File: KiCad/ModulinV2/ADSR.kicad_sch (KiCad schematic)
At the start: 71 parts, among them IC48 TL074HIDR, IC49 AS3310D, IC50 AS3310D

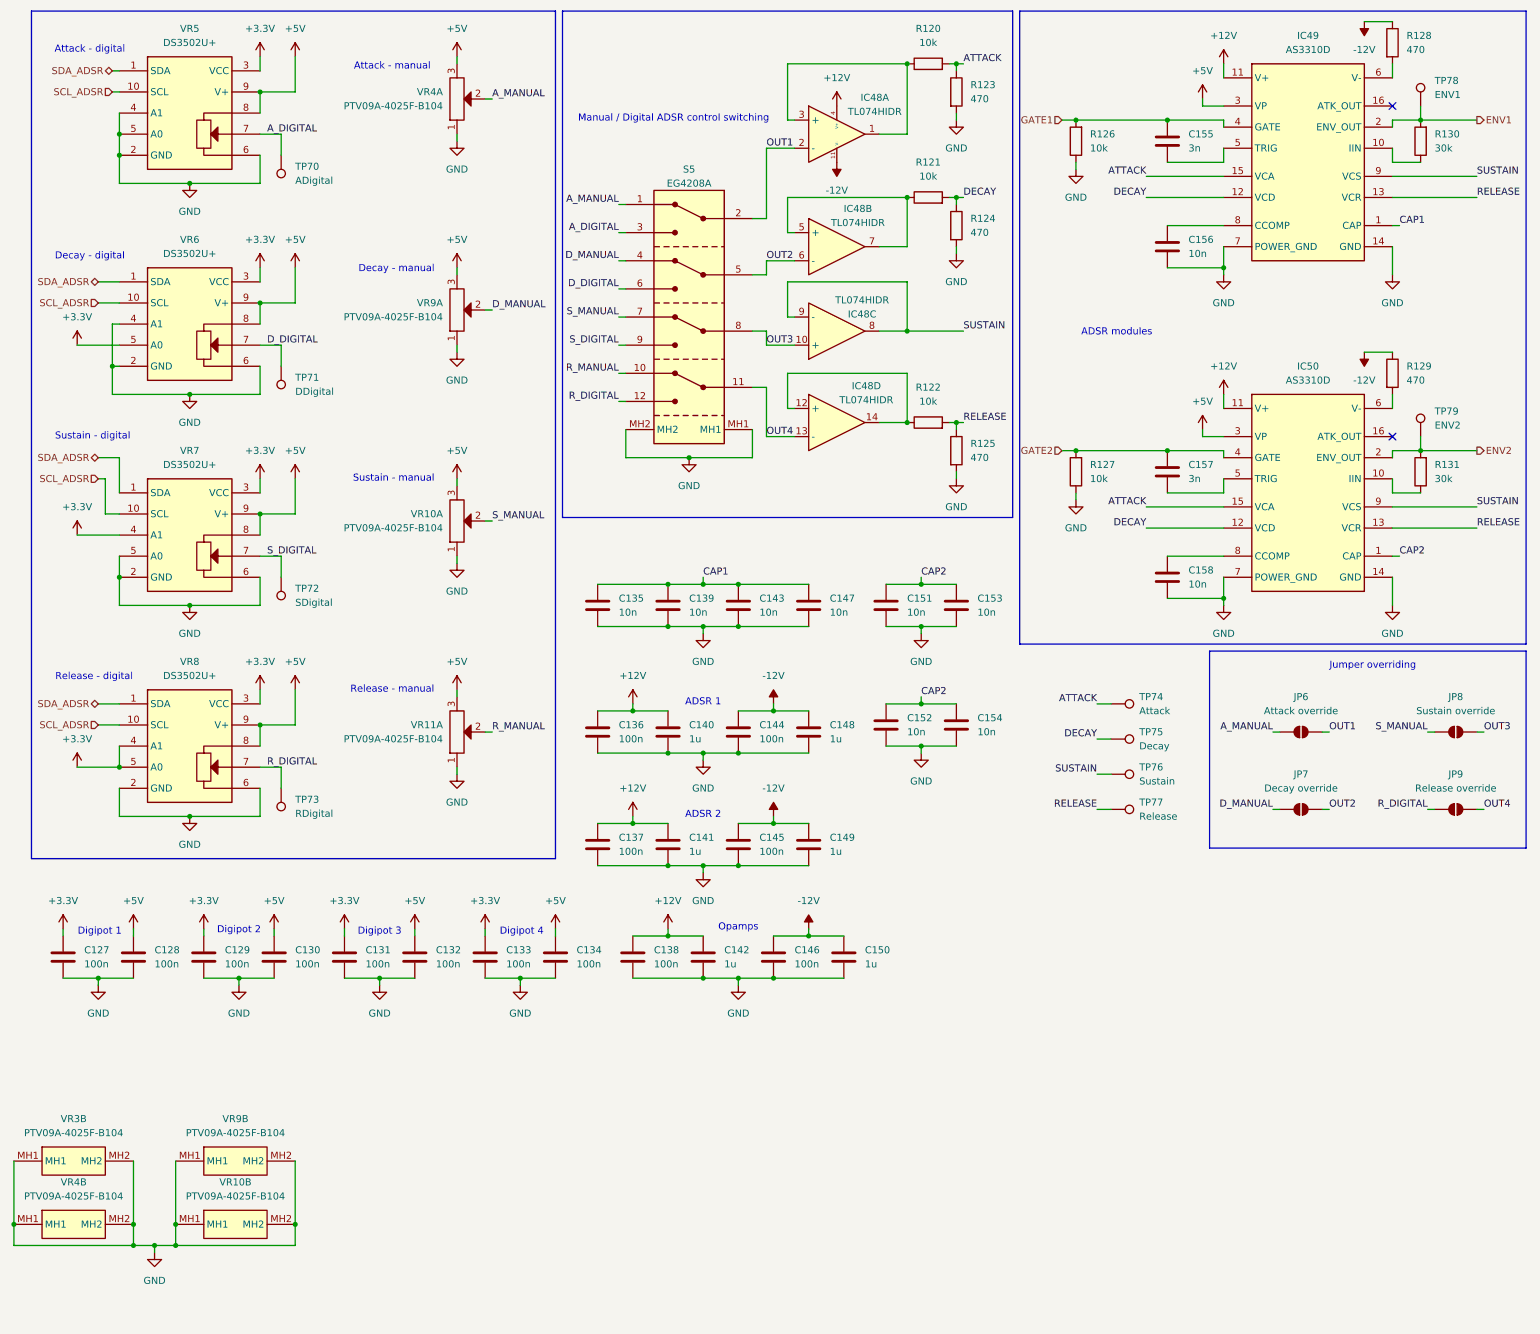
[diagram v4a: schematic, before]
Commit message: Finished Schematic, started on PCB
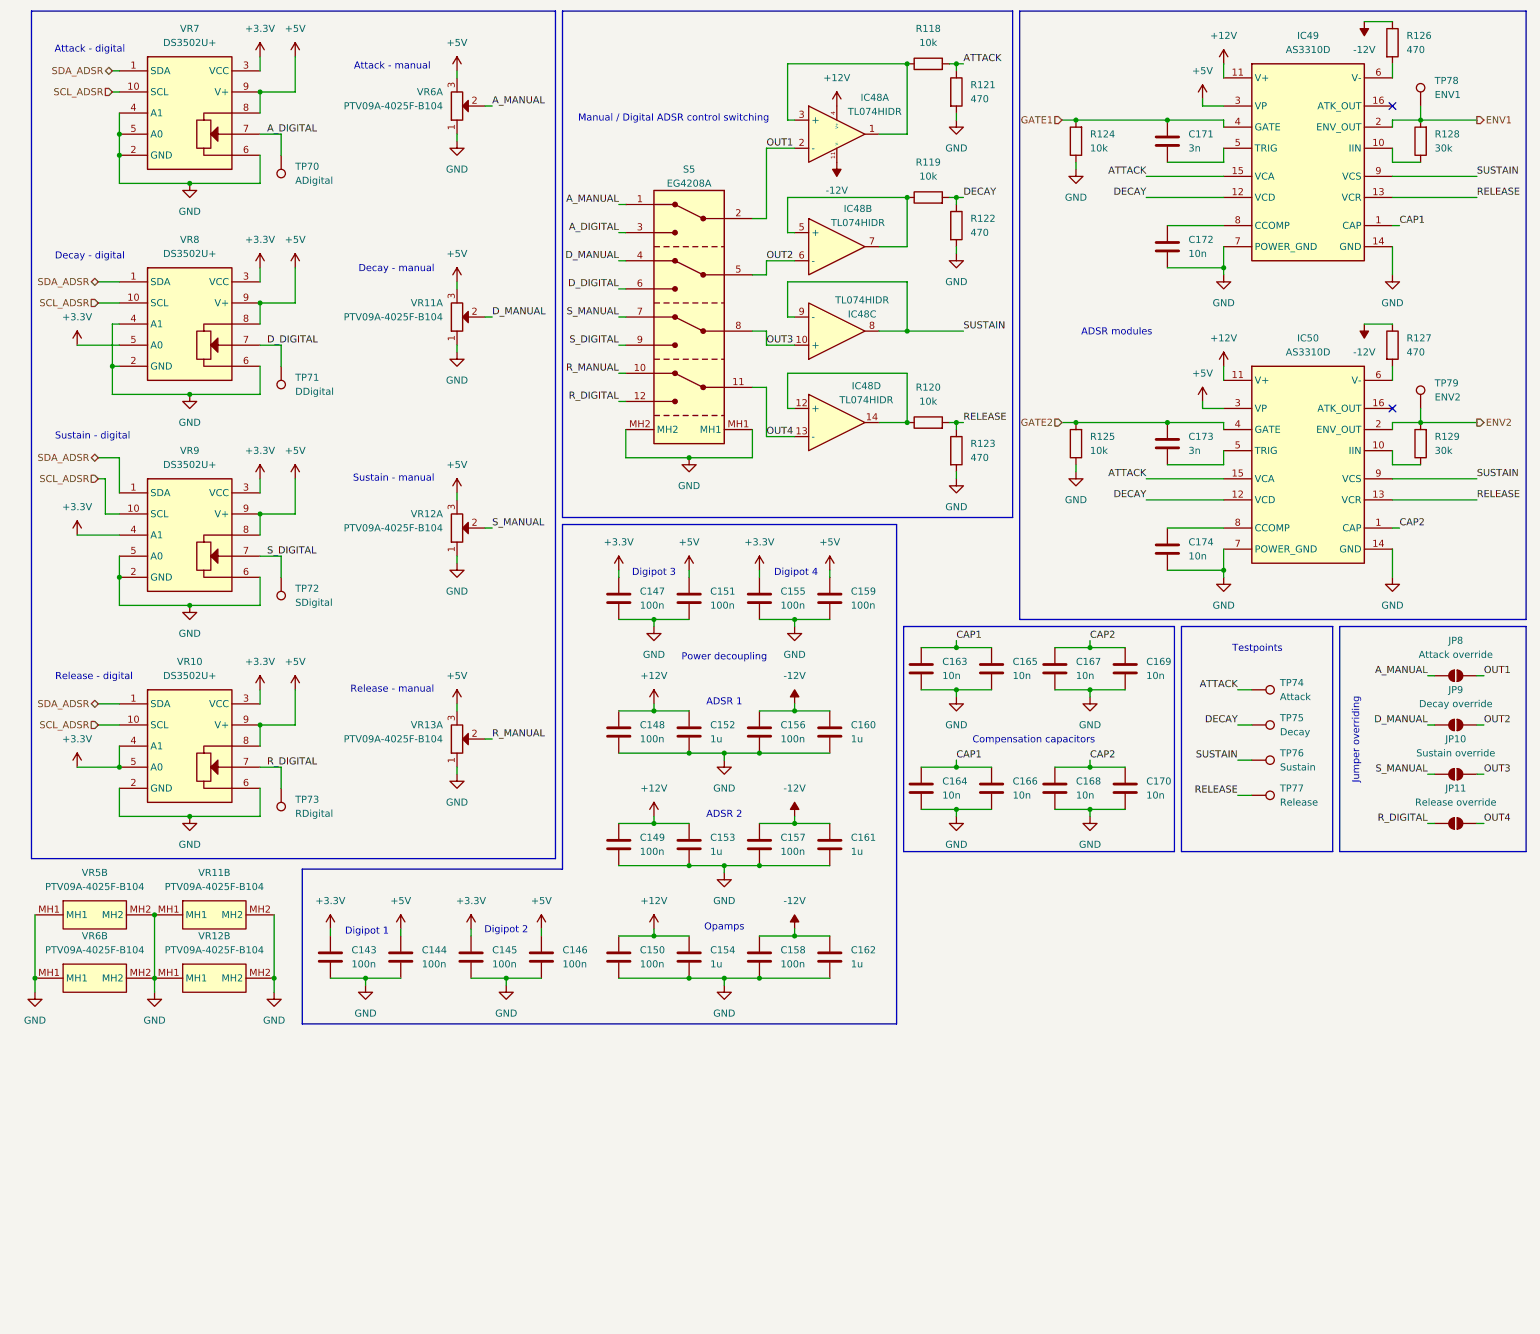
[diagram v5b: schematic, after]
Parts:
- IC49, IC50: footprint SamacSys_Parts:SOIC127P620X175-16N -> Package_SO:SOIC-16_3.9x9.9mm_P1.27mm
- R118: renamed from R120; footprint (none) -> Resistor_SMD:R_0603_1608Metric_Pad0.98x0.95mm_HandSolder
- R119: renamed from R121; footprint (none) -> Resistor_SMD:R_0603_1608Metric_Pad0.98x0.95mm_HandSolder
- R120: renamed from R122; footprint (none) -> Resistor_SMD:R_0603_1608Metric_Pad0.98x0.95mm_HandSolder
- R121: renamed from R123; footprint (none) -> Resistor_SMD:R_0603_1608Metric_Pad0.98x0.95mm_HandSolder
- R122: renamed from R124; footprint (none) -> Resistor_SMD:R_0603_1608Metric_Pad0.98x0.95mm_HandSolder
- R123: renamed from R125; footprint (none) -> Resistor_SMD:R_0603_1608Metric_Pad0.98x0.95mm_HandSolder
- R124: renamed from R126; footprint (none) -> Resistor_SMD:R_0603_1608Metric_Pad0.98x0.95mm_HandSolder
- R125: renamed from R127; footprint (none) -> Resistor_SMD:R_0603_1608Metric_Pad0.98x0.95mm_HandSolder
- R126: renamed from R128; footprint (none) -> Resistor_SMD:R_0603_1608Metric_Pad0.98x0.95mm_HandSolder
- R127: renamed from R129; footprint (none) -> Resistor_SMD:R_0603_1608Metric_Pad0.98x0.95mm_HandSolder
- R128: renamed from R130; footprint (none) -> Resistor_SMD:R_0603_1608Metric_Pad0.98x0.95mm_HandSolder
- R129: renamed from R131; footprint (none) -> Resistor_SMD:R_0603_1608Metric_Pad0.98x0.95mm_HandSolder
- renumbered C127 to C143, C128 to C144, C129 to C145, C130 to C146, C131 to C147, C136 to C148, C137 to C149, C138 to C150, C132 to C151, C140 to C152, C141 to C153, C142 to C154, C133 to C155, C144 to C156, C145 to C157, C146 to C158, C134 to C159, C148 to C160, C149 to C161, C150 to C162, C135 to C163, C143 to C164, C139 to C165, C147 to C166, C151 to C167, C152 to C168, C153 to C169, C154 to C170, C155 to C171, C156 to C172, C157 to C173, C158 to C174, JP8 to JP10, JP9 to JP11, JP6 to JP8, JP7 to JP9, VR8 to VR10, VR9 to VR11, VR10 to VR12, VR11 to VR13, VR3 to VR5, VR4 to VR6, VR5 to VR7, VR6 to VR8, VR7 to VR9
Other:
- note added: "Compensation capacitors"
- note added: "Power decoupling"
- note added: "Testpoints"
- moved on the sheet: C143, C144, C145, C146, C147, C148, C149, C150, C151, C152, C153, C154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

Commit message: Layed out Interface and PWR components and started with MCU layout
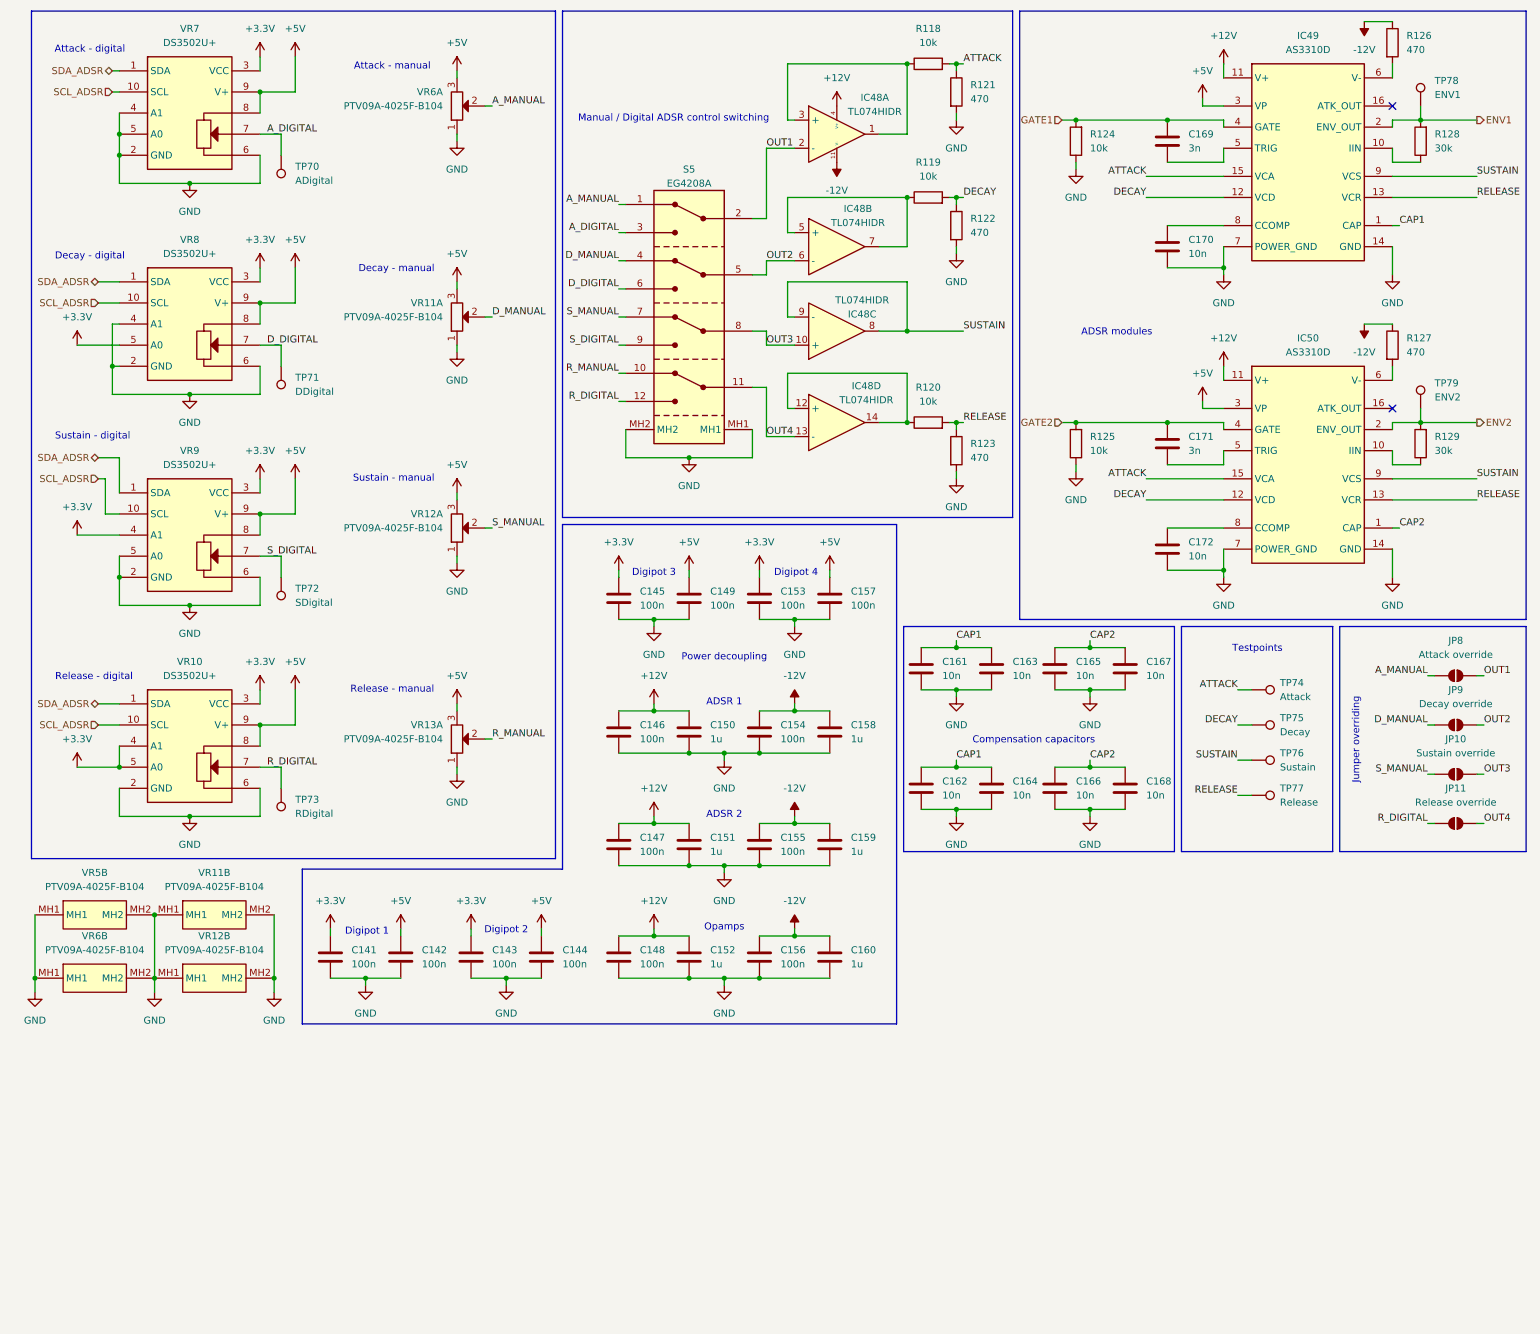
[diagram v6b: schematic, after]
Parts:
- renumbered C143 to C141, C144 to C142, C145 to C143, C146 to C144, C147 to C145, C148 to C146, C149 to C147, C150 to C148, C151 to C149, C152 to C150, C153 to C151, C154 to C152, C155 to C153, C156 to C154, C157 to C155, C158 to C156, C159 to C157, C160 to C158, C161 to C159, C162 to C160, C163 to C161, C164 to C162, C165 to C163, C166 to C164, C167 to C165, C168 to C166, C169 to C167, C170 to C168, C171 to C169, C172 to C170, C173 to C171, C174 to C172
